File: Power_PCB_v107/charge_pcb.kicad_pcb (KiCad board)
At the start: 2 copper layers, 128.1 x 64 mm, 45 parts, among them J1 Mow3, J10 Mot_Left, J11 DC/DC2, J12 DC/DC1, J2 Main_PCB1, J3 Mow2, J4 Battery, J5 Main_PCB2, J6 Power Switch, J7 Mow1, J8 Mot_Right, J9 Start, Q1 BC547C, Q2 IRF9540N, Q3 BC547C, Q4 IRF9540N, U1 INA226, U2 INA226, U3 INA226, U4 INA226, U5 INA226, U6 INA226

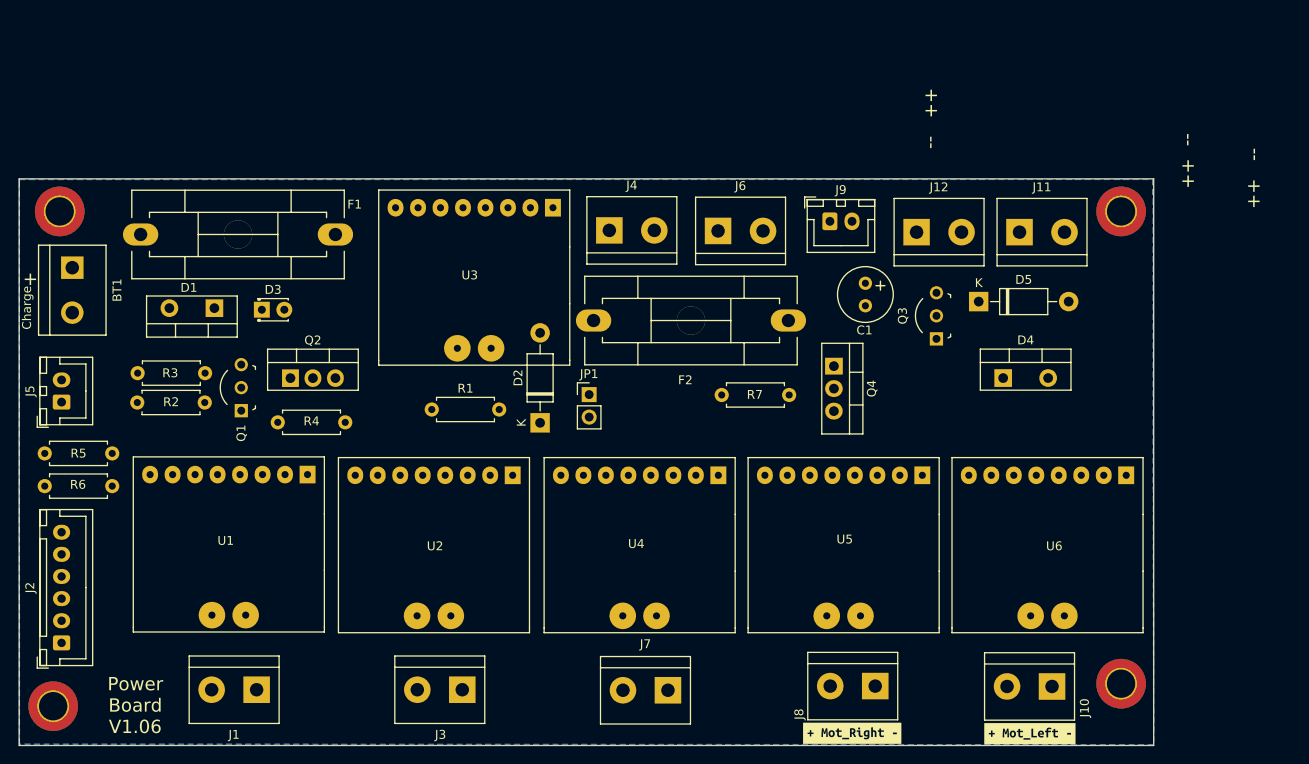
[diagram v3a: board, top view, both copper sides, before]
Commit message: Add Labeling and PCB Routing
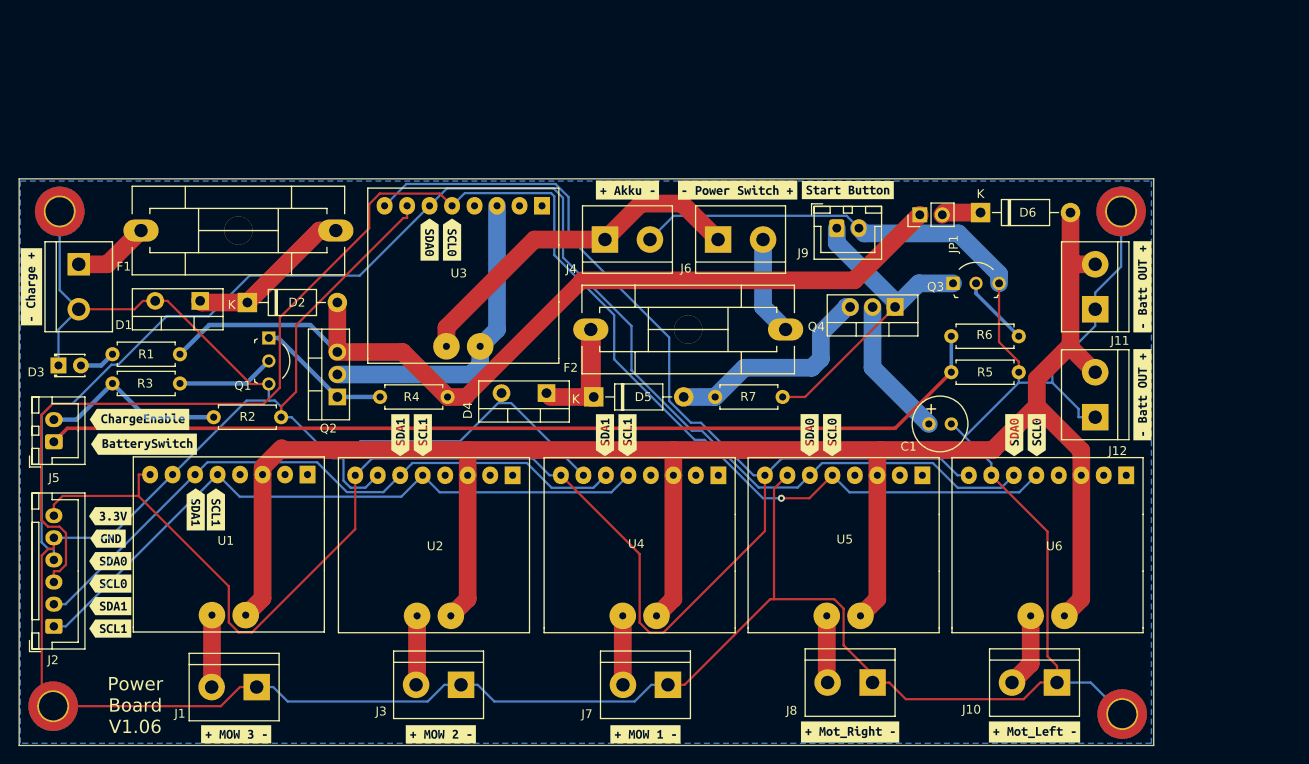
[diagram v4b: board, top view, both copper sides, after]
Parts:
- added D6: SB1240, Diode_THT:D_DO-41_SOD81_P10.16mm_Horizontal, F.Cu at (193.3, 65.0)
- added kibuzzard-630F6257: G***, kibuzzard-630F6257, F.Cu at (155.4, 124.0)
- added kibuzzard-630F629F: G***, kibuzzard-630F629F, F.Cu at (132.3, 124.0)
- added kibuzzard-630F62C6: G***, kibuzzard-630F62C6, F.Cu at (109.2, 124.0)
- added kibuzzard-630F6337: G***, kibuzzard-630F6337, F.Cu at (95.0, 112.0)
- added kibuzzard-630F6348: G***, kibuzzard-630F6348, F.Cu at (95.0, 109.5)
- added kibuzzard-630F68E0: G***, kibuzzard-630F68E0, F.Cu at (95.0, 106.9)
- added kibuzzard-630F6901: G***, kibuzzard-630F6901, F.Cu at (95.0, 104.4)
- added kibuzzard-630F6915: G***, kibuzzard-630F6915, F.Cu at (94.7, 101.9)
- added kibuzzard-630F6938: G***, kibuzzard-630F6938, F.Cu at (95.0, 99.3)
- added kibuzzard-630F6B1E: G***, kibuzzard-630F6B1E, F.Cu at (211.6, 85.6)
- added kibuzzard-630F6B3C: G***, kibuzzard-630F6B3C, F.Cu at (211.6, 73.4)
- added kibuzzard-630F6FC9: G***, kibuzzard-630F6FC9, F.Cu at (178.3, 62.5)
- added kibuzzard-630F70A7: G***, kibuzzard-630F70A7, F.Cu at (165.9, 62.5)
- added kibuzzard-630F7110: G***, kibuzzard-630F7110, F.Cu at (153.4, 62.5)
- added kibuzzard-630F714A: G***, kibuzzard-630F714A, F.Cu at (86.1, 73.4)
- added kibuzzard-630FA3ED: G***, kibuzzard-630FA3ED, F.Cu at (98.8, 91.2)
- added kibuzzard-630FA420: G***, kibuzzard-630FA420, F.Cu at (98.3, 88.4)
- added kibuzzard-630FA50E: G***, kibuzzard-630FA50E, F.Cu at (197.1, 90.2)
- added kibuzzard-630FA52F: G***, kibuzzard-630FA52F, F.Cu at (199.6, 90.2)
- added kibuzzard-630FA55C: G***, kibuzzard-630FA55C, F.Cu at (176.5, 90.2)
- added kibuzzard-630FA573: G***, kibuzzard-630FA573, F.Cu at (174.0, 90.2)
- added kibuzzard-630FA596: G***, kibuzzard-630FA596, F.Cu at (150.9, 90.2)
- added kibuzzard-630FA5B5: G***, kibuzzard-630FA5B5, F.Cu at (153.4, 90.2)
- added kibuzzard-630FA5E0: G***, kibuzzard-630FA5E0, F.Cu at (130.3, 90.2)
- added kibuzzard-630FA5FF: G***, kibuzzard-630FA5FF, F.Cu at (127.8, 90.2)
- added kibuzzard-6311B724: G***, kibuzzard-6311B724, F.Cu at (104.6, 98.6)
- added kibuzzard-6311B760: G***, kibuzzard-6311B760, F.Cu at (106.9, 98.6)
- added kibuzzard-6311B784: G***, kibuzzard-6311B784, F.Cu at (131.1, 68.1)
- added kibuzzard-6311B799: G***, kibuzzard-6311B799, F.Cu at (133.6, 68.1)
- moved R6 103.8 mm to (190.0, 79.0)
- moved R5 102.8 mm to (190.0, 83.1)
- moved D4 51.6 mm to (144.3, 85.4), turned to 180 degrees
- moved D5 44.8 mm to (149.6, 85.9)
- moved JP1 42.5 mm to (186.4, 65.3), turned to 90 degrees
- moved D2 35.7 mm to (110.5, 75.2), turned to 0 degrees
- moved R1 29.1 mm to (102.9, 81.0), turned to 180 degrees
- moved J12 29.0 mm to (206.2, 88.1), turned to 90 degrees
- moved D3 23.8 mm to (89.1, 82.3)
- moved C1 17.4 mm to (187.5, 88.9), turned to 0 degrees
- moved J11 12.2 mm to (206.2, 75.9), turned to 90 degrees
- moved R4 11.9 mm to (133.1, 85.9)
- moved Q4 9.61 mm to (183.6, 75.7), turned to 180 degrees
- moved R2 8.79 mm to (106.7, 88.1)
- moved Q1 8.78 mm to (112.9, 79.2), turned to -90 degrees
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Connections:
- JP1 pad 2: V_Bat -> Net-(D6-Pad1)
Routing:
- net GND: track 0.00 -> 467.9 mm
- net V_Bat: track 0.00 -> 223.5 mm
- net +3V3: track 0.00 -> 218.9 mm
- net SCL0: track 0.00 -> 175.6 mm, vias 0 -> 1
- net SDA0: track 0.00 -> 161.5 mm
- net pinBatterySwitch: track 0.00 -> 108.7 mm
- net Net-(D2-Pad2): track 0.00 -> 102.4 mm
- net SCL1: track 0.00 -> 75.6 mm
- net SDA1: track 0.00 -> 73.5 mm
- net Net-(J4-Pad1): track 0.00 -> 40.3 mm
- net Net-(J9-Pad1): track 0.00 -> 36.2 mm
- net Net-(Q2-Pad2): track 0.00 -> 35.4 mm
- net Net-(D5-Pad2): track 0.00 -> 25.2 mm
- net pinChargeEnable: track 0.00 -> 21.3 mm
- net Net-(C1-Pad1): track 0.00 -> 19.3 mm
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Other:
- board text removed: "+"
- board text removed: "++"
- board text removed: "--"

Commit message: Add Gerber Files
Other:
- board text added: "PowerPCB V1.07"
- board text removed: "Power Board V1.06"
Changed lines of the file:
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@@
       (drillshape 0)
       (scaleselection 1)
-      (outputdirectory "Power_PCB_v106_gerber/")
+      (outputdirectory "./")
     )
   )
@@
     (fp_line (start -0.625 -2.35) (end 0 -1.35) (layer "F.Fab") (width 0.1))
     (fp_line (start -2.45 -2.35) (end -2.45 3.4) (layer "F.Fab") (width 0.1))
-    (pad "1" thru_hole roundrect locked (at 0 0 90) (size 1.7 1.95) (drill 0.95) (layers *.Cu *.Mask) (roundrect_rratio 0.147059)
+    (pad "1" thru_hole roundrect locked (at 0 0 90) (size 1.7 1.95) (drill 0.95) (layers *.Cu *.Mask) (roundrect_rratio 0.1470588235)
       (net 13 "SCL1") (pinfunction "Pin_1") (pintype "passive"))
     (pad "2" thru_hole oval locked (at 2.5 0 90) (size 1.7 1.95) (drill 0.95) (layers *.Cu *.Mask)
@@
     (fp_line (start -2.45 -2.35) (end -2.45 3.4) (layer "F.Fab") (width 0.1))
     (fp_line (start 0 -1.35) (end 0.625 -2.35) (layer "F.Fab") (width 0.1))
-    (pad "1" thru_hole roundrect locked (at 0 0 90) (size 1.7 2) (drill 1) (layers *.Cu *.Mask) (roundrect_rratio 0.147059)
+    (pad "1" thru_hole roundrect locked (at 0 0 90) (size 1.7 2) (drill 1) (layers *.Cu *.Mask) (roundrect_rratio 0.1470588235)
       (net 4 "pinBatterySwitch") (pinfunction "Pin_1") (pintype "passive"))
     (pad "2" thru_hole oval locked (at 2.5 0 90) (size 1.7 2) (drill 1) (layers *.Cu *.Mask)
@@
     (fp_line (start -2.45 -2.35) (end -2.45 3.4) (layer "F.Fab") (width 0.1))
     (fp_line (start 4.95 3.4) (end 4.95 -2.35) (layer "F.Fab") (width 0.1))
-    (pad "1" thru_hole roundrect locked (at 0 0) (size 1.7 2) (drill 1) (layers *.Cu *.Mask) (roundrect_rratio 0.147059)
+    (pad "1" thru_hole roundrect locked (at 0 0) (size 1.7 2) (drill 1) (layers *.Cu *.Mask) (roundrect_rratio 0.1470588235)
       (net 33 "Net-(J9-Pad1)") (pinfunction "Pin_1") (pintype "passive"))
     (pad "2" thru_hole oval locked (at 2.5 0) (size 1.7 2) (drill 1) (layers *.Cu *.Mask)
@@
   (gr_line (start 84.709 61.217) (end 84.709 125.217) (layer "Edge.Cuts") (width 0.15))
   (gr_line (start 212.852 61.217) (end 84.709 61.217) (layer "Edge.Cuts") (width 0.15))
-  (gr_text "Power\nBoard\nV1.06" (at 97.83 120.7) (layer "F.SilkS")
+  (gr_text "PowerPCB\nV1.07" (at 96.774 117.856) (layer "F.SilkS")
     (effects (font (size 1.5 1.5) (thickness 0.3)))
   )
